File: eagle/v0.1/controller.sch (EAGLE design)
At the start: 22 parts, among them J1 61729-1011, Q2 4M9152

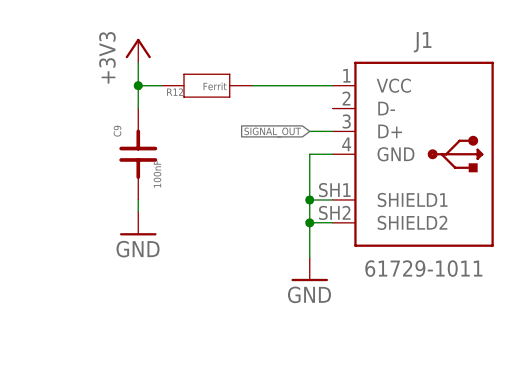
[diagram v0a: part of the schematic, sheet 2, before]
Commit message: add usb type c
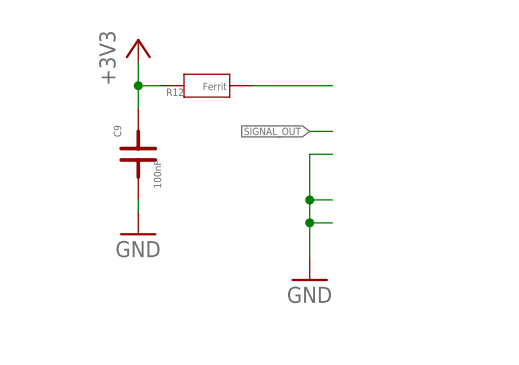
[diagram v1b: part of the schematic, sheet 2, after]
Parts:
- removed J1: 61729-1011, Connector_USB:61729-1011
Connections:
- removed net SHIELD1: J1.GND, J1.SHIELD1, J1.SHIELD2
- net N$1: no longer J1.VCC
- net SIGNAL_OUT: no longer J1.D+
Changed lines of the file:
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@@
 <setting verticaltext="up"/>
 </settings>
-<grid distance="50" unitdist="mil" unit="mil" style="dots" multiple="1" display="yes" altdistance="0.01" altunitdist="inch" altunit="inch"/>
+<grid distance="0.1" unitdist="inch" unit="inch" style="lines" multiple="1" display="no" altdistance="0.01" altunitdist="inch" altunit="inch"/>
 <layers>
 <layer number="1" name="Top" color="4" fill="1" visible="no" active="no"/>
@@
 <part name="+3V4" library="supply1" library_urn="urn:adsk.eagle:library:371" deviceset="+3V3" device=""/>
 <part name="+3V5" library="supply1" library_urn="urn:adsk.eagle:library:371" deviceset="+3V3" device=""/>
-<part name="J1" library="Connector_USB" library_urn="urn:adsk.eagle:library:27510300" deviceset="61729-1011" device="" package3d_urn="urn:adsk.eagle:package:27659501/2"/>
 </parts>
 <sheets>
@@
 <instance part="+3V2" gate="G$1" x="25.4" y="163.83" smashed="yes">
 <attribute name="VALUE" x="22.86" y="158.75" size="1.778" layer="96" rot="R90"/>
-</instance>
-<instance part="J1" gate="G$1" x="245.11" y="156.21" smashed="yes">
-<attribute name="NAME" x="245.11" y="168.91" size="1.778" layer="95" align="center"/>
-<attribute name="VALUE" x="245.11" y="143.51" size="1.778" layer="96" align="center"/>
 </instance>
 </instances>
@@
 <pinref part="GND6" gate="1" pin="GND"/>
 </segment>
+<segment>
+<wire x1="232.41" y1="144.78" x2="232.41" y2="148.59" width="0.1524" layer="91"/>
+<wire x1="232.41" y1="148.59" x2="232.41" y2="151.13" width="0.1524" layer="91"/>
+<wire x1="232.41" y1="151.13" x2="234.95" y2="151.13" width="0.1524" layer="91"/>
+<wire x1="234.95" y1="156.21" x2="232.41" y2="156.21" width="0.1524" layer="91"/>
+<wire x1="232.41" y1="156.21" x2="232.41" y2="151.13" width="0.1524" layer="91"/>
+<junction x="232.41" y="151.13"/>
+<pinref part="GND5" gate="1" pin="GND"/>
+<wire x1="232.41" y1="148.59" x2="234.95" y2="148.59" width="0.1524" layer="91"/>
+<junction x="232.41" y="148.59"/>
+</segment>
 </net>
 <net name="+3.3V" class="0">
@@
 <pinref part="R12" gate="G$1" pin="1"/>
 <wire x1="234.95" y1="163.83" x2="226.06" y2="163.83" width="0.1524" layer="91"/>
-<pinref part="J1" gate="G$1" pin="VCC"/>
 </segment>
 </net>
@@
 <wire x1="234.95" y1="158.75" x2="232.41" y2="158.75" width="0.1524" layer="91"/>
 <label x="232.41" y="158.75" size="0.8128" layer="95" rot="R180" xref="yes"/>
-<pinref part="J1" gate="G$1" pin="D+"/>
-</segment>
-</net>
-<net name="SHIELD1" class="0">
-<segment>
-<wire x1="232.41" y1="144.78" x2="232.41" y2="148.59" width="0.1524" layer="91"/>
-<wire x1="232.41" y1="148.59" x2="232.41" y2="151.13" width="0.1524" layer="91"/>
-<wire x1="232.41" y1="151.13" x2="234.95" y2="151.13" width="0.1524" layer="91"/>
-<wire x1="234.95" y1="156.21" x2="232.41" y2="156.21" width="0.1524" layer="91"/>
-<wire x1="232.41" y1="156.21" x2="232.41" y2="151.13" width="0.1524" layer="91"/>
-<junction x="232.41" y="151.13"/>
-<pinref part="GND5" gate="1" pin="GND"/>
-<pinref part="J1" gate="G$1" pin="GND"/>
-<pinref part="J1" gate="G$1" pin="SHIELD1"/>
-<pinref part="J1" gate="G$1" pin="SHIELD2"/>
-<wire x1="232.41" y1="148.59" x2="234.95" y2="148.59" width="0.1524" layer="91"/>
-<junction x="232.41" y="148.59"/>
-</segment>
-</net>
+</segment>
+</net>
